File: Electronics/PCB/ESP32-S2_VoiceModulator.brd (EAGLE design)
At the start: 160 x 100 mm, 17 parts, among them IC1 ESP32-S2, IC2 AT25SF041-SSHD-B, J1 0532610671, Y1 FA-20H_40.0000MF15Z-AC3

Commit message: CHanged labelign for VCC/ power
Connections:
- new net VCC: C10.1, C11.1, C4.1, C5.1, C6.1, C7.1, C8.1, C9.1, IC1.1, IC1.3, IC1.4, IC1.45, IC1.51, IC1.54, IC2.8, R1.2, R2.2
- net +3V3: no longer C10.1, C11.1, C4.1, C5.1, C6.1, C7.1, C8.1, C9.1, IC1.1, IC1.3, IC1.4, IC1.45, IC1.51, IC1.54, IC2.8, R1.2, R2.2
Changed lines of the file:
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@@
 </signal>
 <signal name="+3V3">
-<contactref element="IC2" pad="8"/>
-<contactref element="C10" pad="1"/>
-<contactref element="R2" pad="2"/>
-<contactref element="C4" pad="1"/>
-<contactref element="C5" pad="1"/>
-<contactref element="C7" pad="1"/>
-<contactref element="C8" pad="1"/>
-<contactref element="C9" pad="1"/>
-<contactref element="C11" pad="1"/>
-<contactref element="C6" pad="1"/>
-<contactref element="IC1" pad="54"/>
-<contactref element="IC1" pad="51"/>
-<contactref element="IC1" pad="45"/>
 <contactref element="IC1" pad="20"/>
 <contactref element="IC1" pad="27"/>
 <contactref element="IC1" pad="30"/>
-<contactref element="IC1" pad="4"/>
-<contactref element="IC1" pad="3"/>
-<contactref element="IC1" pad="1"/>
-<contactref element="R1" pad="2"/>
-<wire x1="1.35" y1="-28" x2="1.35" y2="-33" width="0" layer="19" extent="1-1"/>
-<wire x1="1.35" y1="-23" x2="1.35" y2="-28" width="0" layer="19" extent="1-1"/>
-<wire x1="1.15" y1="-18" x2="1.35" y2="-23" width="0" layer="19" extent="1-1"/>
-<wire x1="4.4" y1="-8.45" x2="1.15" y2="-18" width="0" layer="19" extent="1-1"/>
 <wire x1="7.2" y1="-8.45" x2="4.4" y2="-8.45" width="0" layer="19" extent="1-1"/>
 <wire x1="8.45" y1="-7.2" x2="7.2" y2="-8.45" width="0" layer="19" extent="1-1"/>
-<wire x1="1.55" y1="-3.6" x2="4.4" y2="-8.45" width="0" layer="19" extent="1-1"/>
-<wire x1="1.55" y1="-3.2" x2="1.55" y2="-3.6" width="0" layer="19" extent="1-1"/>
-<wire x1="1.55" y1="-2.4" x2="1.55" y2="-3.2" width="0" layer="19" extent="1-1"/>
-<wire x1="3.2" y1="-1.55" x2="1.55" y2="-2.4" width="0" layer="19" extent="1-1"/>
-<wire x1="4.4" y1="-1.55" x2="3.2" y2="-1.55" width="0" layer="19" extent="1-1"/>
-<wire x1="6.8" y1="-1.55" x2="4.4" y2="-1.55" width="0" layer="19" extent="1-1"/>
-<wire x1="16.15" y1="-18" x2="7.2" y2="-8.45" width="0" layer="19" extent="1-1"/>
-<wire x1="16.35" y1="-23" x2="16.15" y2="-18" width="0" layer="19" extent="1-1"/>
-<wire x1="16.35" y1="-28" x2="16.35" y2="-23" width="0" layer="19" extent="1-1"/>
-<wire x1="16.35" y1="-33" x2="16.35" y2="-28" width="0" layer="19" extent="1-1"/>
-<wire x1="16.85" y1="-43" x2="16.35" y2="-33" width="0" layer="19" extent="1-1"/>
-<wire x1="24.85" y1="-43" x2="16.85" y2="-43" width="0" layer="19" extent="1-1"/>
-<wire x1="22.712" y1="-1.095" x2="8.45" y2="-7.2" width="0" layer="19" extent="1-1"/>
 </signal>
 <signal name="SPID">
@@
 <wire x1="1.55" y1="-4" x2="8.875" y2="-46.996" width="0" layer="19" extent="1-1"/>
 </signal>
+<signal name="VCC">
+<contactref element="IC1" pad="4"/>
+<contactref element="IC1" pad="3"/>
+<contactref element="IC1" pad="1"/>
+<contactref element="R1" pad="2"/>
+<contactref element="IC1" pad="54"/>
+<contactref element="IC1" pad="51"/>
+<contactref element="IC1" pad="45"/>
+<contactref element="R2" pad="2"/>
+<contactref element="IC2" pad="8"/>
+<contactref element="C10" pad="1"/>
+<contactref element="C4" pad="1"/>
+<contactref element="C5" pad="1"/>
+<contactref element="C7" pad="1"/>
+<contactref element="C8" pad="1"/>
+<contactref element="C9" pad="1"/>
+<contactref element="C11" pad="1"/>
+<contactref element="C6" pad="1"/>
+<wire x1="1.35" y1="-28" x2="1.35" y2="-33" width="0" layer="19" extent="1-1"/>
+<wire x1="1.35" y1="-23" x2="1.35" y2="-28" width="0" layer="19" extent="1-1"/>
+<wire x1="1.15" y1="-18" x2="1.35" y2="-23" width="0" layer="19" extent="1-1"/>
+<wire x1="1.55" y1="-3.6" x2="1.15" y2="-18" width="0" layer="19" extent="1-1"/>
+<wire x1="1.55" y1="-3.2" x2="1.55" y2="-3.6" width="0" layer="19" extent="1-1"/>
+<wire x1="1.55" y1="-2.4" x2="1.55" y2="-3.2" width="0" layer="19" extent="1-1"/>
+<wire x1="3.2" y1="-1.55" x2="1.55" y2="-2.4" width="0" layer="19" extent="1-1"/>
+<wire x1="4.4" y1="-1.55" x2="3.2" y2="-1.55" width="0" layer="19" extent="1-1"/>
+<wire x1="6.8" y1="-1.55" x2="4.4" y2="-1.55" width="0" layer="19" extent="1-1"/>
+<wire x1="16.35" y1="-33" x2="1.35" y2="-33" width="0" layer="19" extent="1-1"/>
+<wire x1="16.35" y1="-28" x2="16.35" y2="-33" width="0" layer="19" extent="1-1"/>
+<wire x1="16.35" y1="-23" x2="16.35" y2="-28" width="0" layer="19" extent="1-1"/>
+<wire x1="16.15" y1="-18" x2="16.35" y2="-23" width="0" layer="19" extent="1-1"/>
+<wire x1="16.85" y1="-43" x2="16.35" y2="-33" width="0" layer="19" extent="1-1"/>
+<wire x1="24.85" y1="-43" x2="16.85" y2="-43" width="0" layer="19" extent="1-1"/>
+<wire x1="22.712" y1="-1.095" x2="6.8" y2="-1.55" width="0" layer="19" extent="1-1"/>
+</signal>
 <signal name="+5V">

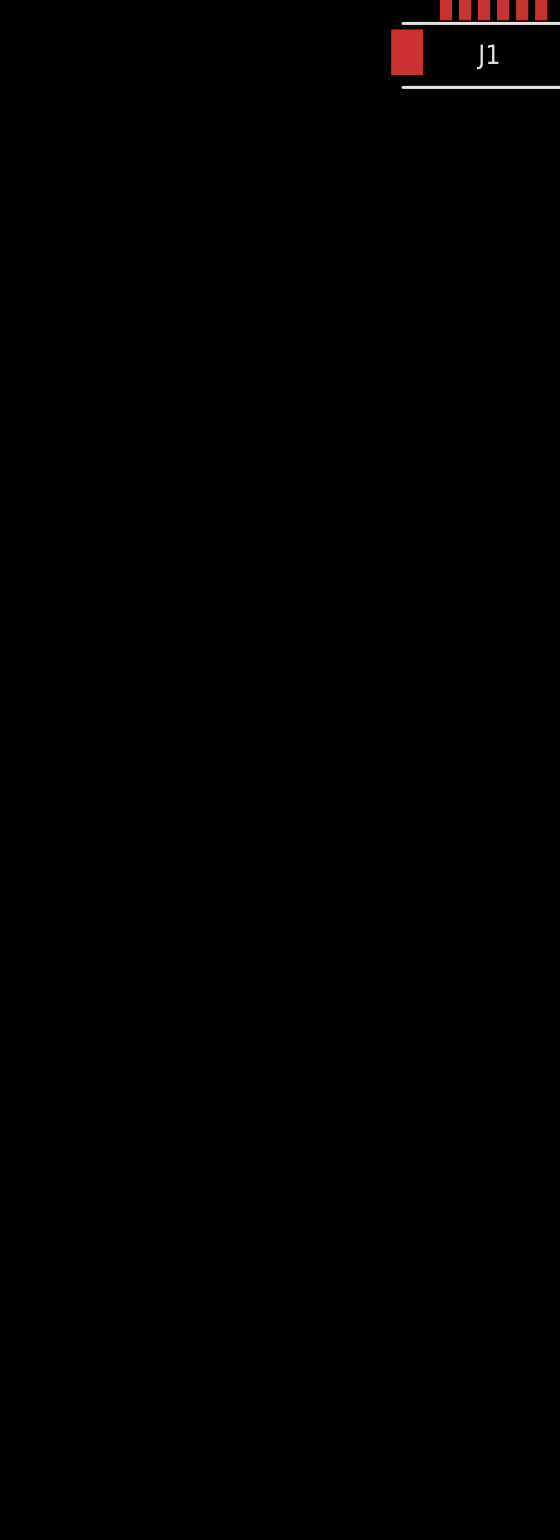
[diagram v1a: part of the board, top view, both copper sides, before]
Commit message: Added schematic drawing for the microphone emulation and PCB microphone adjustment.
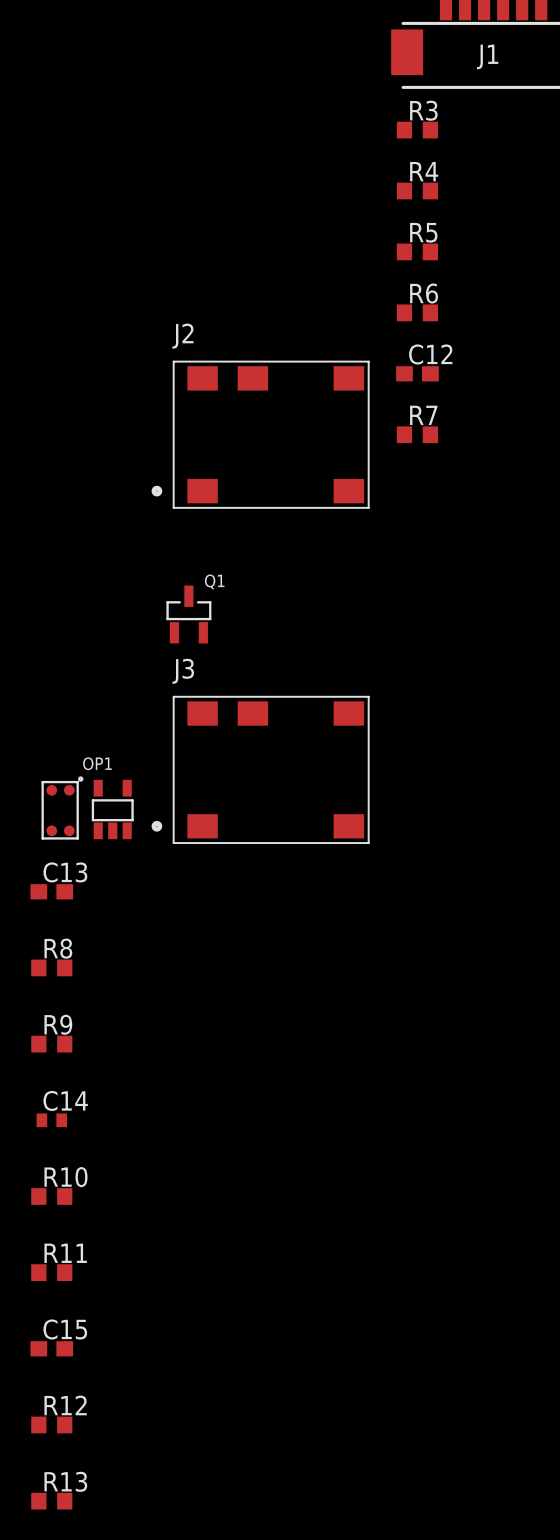
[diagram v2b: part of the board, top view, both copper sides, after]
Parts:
- added C12, C13, C15: 1uF/6.3V, resistor:C0603
- added C14: 0.1µF/16V, rcl:C0402
- added J2, J3: (no value), VoiceModulator:SJ2-35364B-SMT-TR
- added MK1: WMM7022AT0, VoiceModulator:WMM7022AT0
- added OP1: MCP6001T-I/OT, VoiceModulator:SOT-23-5
- added Q1: CPH3910, VoiceModulator:SOT-23-3
- added R10, R9: 1K, resistor:R0603
- added R11: 70k, resistor:R0603
- added R12, R13, R8: 100K, resistor:R0603
- added R3, R5, R6, R7: 10K, resistor:R0603
- added R4: 100R, resistor:R0603
- C1, C10, C11, C6, C7, C8, C9: value 0.1µF/16V/X7R -> 0.1µF/16V
- C2, C3: value 9pF/6.3V/X7R -> 9pF/6.3V
- C4, C5: value 10µF/6.3V/X7R -> 10µF/6.3V
- R1, R2: value 10K/5% -> 10K
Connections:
- new net AGND: J2.4, J3.4, Q1.P$1, R5.2
- new net AUDIO_LEFT: J2.2, J3.2
- new net AUDIO_RIGHT: J2.3, J3.3
- new net DAC_OUTPUT: R3.2
- new net HEADPHONE_SWITCH: J2.10
- new net MICROPHONE_HEADSET: J2.1
- new net MICROPHONE_OUT: J3.1, R6.1, R7.2
- new net N$1: C12.2, Q1.P$3, R5.1
- new net N$2: C12.1, R3.1, R4.2
- new net N$3: C13.2, OP1.P$3, R8.1, R9.2
- new net N$4: C13.1, MK1.4
- new net N$5: Q1.P$2, R6.2, R7.1
- new net N$6: OP1.P$4, R10.2, R11.2
- new net N$7: C15.1, OP1.P$1, R11.1
- new net PCB-MICROPHONE_OUTPUT: C15.2, R12.2, R13.1
- new net PHONE_SWITCH: J3.10
- net +5V: now also OP1.P$5
- net GND: now also C14.2, MK1.2, MK1.3, OP1.P$2, R10.1, R12.1, R4.1, R9.1
- net VCC: now also C14.1, MK1.1, R13.2, R8.2

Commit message: Added DC/DC
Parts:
- added C16, C17: 1uF/6.3V, resistor:C0603
- added IC3: MIC5504-3.3YM5-TR, VoiceModulator:SOT-23-5
- J2, J3: value (none) -> SJ2-35364B-SMT-TR
- moved OP1 57.9 mm to (-36.0, -156.0)
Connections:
- net +5V: now also C16.1, IC3.P$1, IC3.P$3
- net GND: now also C16.2, C17.2, IC3.P$2
- net VCC: now also C17.1, IC3.P$5
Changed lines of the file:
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@@
 <attribute name="VALUE" x="1.365" y="-76.905" size="1.27" layer="27"/>
 </element>
-<element name="J2" library="VoiceModulator" package="SJ2-35364B-SMT-TR" value="" x="-14" y="-75" smashed="yes">
+<element name="J2" library="VoiceModulator" package="SJ2-35364B-SMT-TR" value="SJ2-35364B-SMT-TR" x="-14" y="-75" smashed="yes">
 <attribute name="NAME" x="-14" y="-68.9989" size="1.27023125" layer="25"/>
 <attribute name="VALUE" x="-14" y="-81.002440625" size="1.27051875" layer="27" align="top-left"/>
@@
 <attribute name="NAME" x="-12" y="-85" size="0.8128" layer="25"/>
 </element>
-<element name="J3" library="VoiceModulator" package="SJ2-35364B-SMT-TR" value="" x="-14" y="-97" smashed="yes">
+<element name="J3" library="VoiceModulator" package="SJ2-35364B-SMT-TR" value="SJ2-35364B-SMT-TR" x="-14" y="-97" smashed="yes">
 <attribute name="NAME" x="-14" y="-90.9989" size="1.27023125" layer="25"/>
 <attribute name="VALUE" x="-14" y="-103.002440625" size="1.27051875" layer="27" align="top-left"/>
-</element>
-<element name="OP1" library="VoiceModulator" package="SOT-23-5" value="MCP6001T-I/OT" x="-18" y="-101" smashed="yes">
-<attribute name="NAME" x="-20" y="-97" size="0.8128" layer="25"/>
 </element>
 <element name="MK1" library="VoiceModulator" package="WMM7022AT0" value="WMM7022AT0" x="-22" y="-101" smashed="yes"/>
@@
 <attribute name="NAME" x="-22.635" y="-144.365" size="1.27" layer="25"/>
 <attribute name="VALUE" x="-22.635" y="-146.905" size="1.27" layer="27"/>
+</element>
+<element name="C16" library="resistor" library_urn="urn:adsk.eagle:library:348" package="C0603" package3d_urn="urn:adsk.eagle:package:23616/2" value="1uF/6.3V" x="-27" y="-150" smashed="yes">
+<attribute name="NAME" x="-27.635" y="-149.365" size="1.27" layer="25"/>
+<attribute name="VALUE" x="-27.635" y="-151.905" size="1.27" layer="27"/>
+</element>
+<element name="C17" library="resistor" library_urn="urn:adsk.eagle:library:348" package="C0603" package3d_urn="urn:adsk.eagle:package:23616/2" value="1uF/6.3V" x="-27" y="-155" smashed="yes">
+<attribute name="NAME" x="-27.635" y="-154.365" size="1.27" layer="25"/>
+<attribute name="VALUE" x="-27.635" y="-156.905" size="1.27" layer="27"/>
+</element>
+<element name="IC3" library="VoiceModulator" package="SOT-23-5" value="MIC5504-3.3YM5-TR" x="-31" y="-156" smashed="yes">
+<attribute name="NAME" x="-33" y="-152" size="0.8128" layer="25"/>
+</element>
+<element name="OP1" library="VoiceModulator" package="SOT-23-5" value="MCP6001T-I/OT" x="-36" y="-156" smashed="yes">
+<attribute name="NAME" x="-38" y="-152" size="0.8128" layer="25"/>
 </element>
 </elements>
@@
 <contactref element="C14" pad="2"/>
 <contactref element="R10" pad="1"/>
+<contactref element="R12" pad="1"/>
+<contactref element="C16" pad="2"/>
+<contactref element="C17" pad="2"/>
+<contactref element="IC3" pad="P$2"/>
 <contactref element="OP1" pad="P$2"/>
-<contactref element="R12" pad="1"/>
+<wire x1="-31" y1="-156" x2="-36" y2="-156" width="0" layer="19" extent="1-1"/>
+<wire x1="-26.15" y1="-155" x2="-31" y2="-156" width="0" layer="19" extent="1-1"/>
+<wire x1="-26.15" y1="-150" x2="-26.15" y2="-155" width="0" layer="19" extent="1-1"/>
+<wire x1="-22.85" y1="-140" x2="-26.15" y2="-150" width="0" layer="19" extent="1-1"/>
 <wire x1="-22.85" y1="-125" x2="-22.85" y2="-140" width="0" layer="19" extent="1-1"/>
 <wire x1="-21.35" y1="-120" x2="-22.85" y2="-125" width="0" layer="19" extent="1-1"/>
@@
 <wire x1="-22" y1="-101" x2="-22.85" y2="-115" width="0" layer="19" extent="1-1"/>
 <wire x1="-20.85" y1="-101" x2="-22" y2="-101" width="0" layer="19" extent="1-1"/>
-<wire x1="-18" y1="-101" x2="-20.85" y2="-101" width="0" layer="19" extent="1-1"/>
-<wire x1="1.15" y1="-59" x2="-18" y2="-101" width="0" layer="19" extent="1-1"/>
+<wire x1="1.15" y1="-59" x2="-20.85" y2="-101" width="0" layer="19" extent="1-1"/>
 <wire x1="10.125" y1="-46.996" x2="1.15" y2="-59" width="0" layer="19" extent="1-1"/>
 <wire x1="2.85" y1="-43" x2="10.125" y2="-46.996" width="0" layer="19" extent="1-1"/>
@@
 <contactref element="IC1" pad="51"/>
 <contactref element="IC1" pad="45"/>
-<contactref element="R2" pad="2"/>
 <contactref element="IC2" pad="8"/>
 <contactref element="C10" pad="1"/>
@@
 <contactref element="C14" pad="1"/>
 <contactref element="R13" pad="2"/>
+<contactref element="C17" pad="1"/>
+<contactref element="IC3" pad="P$5"/>
+<contactref element="R2" pad="2"/>
+<wire x1="-27.85" y1="-155" x2="-31.95" y2="-153.2" width="0" layer="19" extent="1-1"/>
+<wire x1="-21.15" y1="-145" x2="-27.85" y2="-155" width="0" layer="19" extent="1-1"/>
 <wire x1="-22.65" y1="-120" x2="-21.15" y2="-145" width="0" layer="19" extent="1-1"/>
 <wire x1="-21.15" y1="-110" x2="-22.65" y2="-120" width="0" layer="19" extent="1-1"/>
@@
 <signal name="+5V">
 <contactref element="J1" pad="1"/>
+<contactref element="C16" pad="1"/>
+<contactref element="IC3" pad="P$1"/>
+<contactref element="IC3" pad="P$3"/>
 <contactref element="OP1" pad="P$5"/>
-<wire x1="3.875" y1="-46.996" x2="-18.95" y2="-98.2" width="0" layer="19" extent="1-1"/>
+<wire x1="-31.95" y1="-156" x2="-36.95" y2="-153.2" width="0" layer="19" extent="1-1"/>
+<wire x1="-30.05" y1="-156" x2="-31.95" y2="-156" width="0" layer="19" extent="1-1"/>
+<wire x1="-27.85" y1="-150" x2="-30.05" y2="-156" width="0" layer="19" extent="1-1"/>
+<wire x1="3.875" y1="-46.996" x2="-27.85" y2="-150" width="0" layer="19" extent="1-1"/>
 </signal>
 <signal name="N$1">
@@
 <contactref element="R9" pad="2"/>
 <contactref element="OP1" pad="P$3"/>
+<wire x1="-21.15" y1="-115" x2="-35.05" y2="-156" width="0" layer="19" extent="1-1"/>
 <wire x1="-22.85" y1="-110" x2="-21.15" y2="-115" width="0" layer="19" extent="1-1"/>
 <wire x1="-21.15" y1="-105" x2="-22.85" y2="-110" width="0" layer="19" extent="1-1"/>
-<wire x1="-17.05" y1="-101" x2="-21.15" y2="-105" width="0" layer="19" extent="1-1"/>
 </signal>
 <signal name="N$6">
 <contactref element="R10" pad="2"/>
+<contactref element="R11" pad="2"/>
 <contactref element="OP1" pad="P$4"/>
-<contactref element="R11" pad="2"/>
+<wire x1="-21.15" y1="-130" x2="-35.05" y2="-153.2" width="0" layer="19" extent="1-1"/>
 <wire x1="-21.15" y1="-125" x2="-21.15" y2="-130" width="0" layer="19" extent="1-1"/>
-<wire x1="-17.05" y1="-98.2" x2="-21.15" y2="-125" width="0" layer="19" extent="1-1"/>
 </signal>
 <signal name="N$7">
 <contactref element="R11" pad="1"/>
+<contactref element="C15" pad="1"/>
 <contactref element="OP1" pad="P$1"/>
-<contactref element="C15" pad="1"/>
+<wire x1="-22.85" y1="-135" x2="-36.95" y2="-156" width="0" layer="19" extent="1-1"/>
 <wire x1="-22.85" y1="-130" x2="-22.85" y2="-135" width="0" layer="19" extent="1-1"/>
-<wire x1="-18.95" y1="-101" x2="-22.85" y2="-130" width="0" layer="19" extent="1-1"/>
 </signal>
 <signal name="PCB-MICROPHONE_OUTPUT">

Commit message: Minor changes to schematic
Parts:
- removed J1: 0532610671, SamacSys_Parts:0532610671
- added C18: 0.1µF/16V, resistor:C0603
- added C19: 0.1µF/16V, rcl:C0402
- added C20: 1uF/6.3V, resistor:C0603
- added C21: 10µF/6.3V, rcl:C0603
- added J4: 10118192-0002LF, VoiceModulator:CONN_10118192-0002LF_AMP
- added OP2: MCP6001T-I/OT, VoiceModulator:SOT-23-5
- added R14, R18, R19, R20: 100K, resistor:R0603
- added R15, R16: 1K, resistor:R0603
- added R17: 70k, resistor:R0603
- added TAG_CONNECT_ICSP_HEADER: TAG-CONNECT_PADS, TAG-CONNECT_PADS-lbr:TAG-CONNECT_PADS
- R3: value 10K -> 100K
- R4: value 100R -> 1k
- moved C16 204.2 mm to (-19.0, 54.0)
- moved C17 204.2 mm to (-19.0, 49.0)
- moved OP1 184.6 mm to (13.0, 22.0)
- moved R13 177.3 mm to (-12.0, 32.0)
- moved C15 172.1 mm to (-15.0, 37.0)
- moved R12 172.0 mm to (-18.0, 32.0)
- moved IC3 171.9 mm to (19.7, 8.30), turned to 90 degrees
- moved C14 164.0 mm to (-20.0, 44.0)
- moved R11 157.0 mm to (-19.0, 27.0)
- moved R10 152.0 mm to (-24.0, 27.0)
- moved J3 144.5 mm to (7.00, 46.0), turned to 270 degrees
- moved R9 142.2 mm to (-14.0, 27.0)
- moved R8 142.0 mm to (-24.0, 32.0)
- moved C13 130.4 mm to (15.0, 20.0), turned to 90 degrees
- moved MK1 126.4 mm to (11.0, 21.0), turned to 270 degrees
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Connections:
- removed net AGND: J2.4, J3.4, Q1.P$1, R5.2
- new net D+: IC1.25, J4.3
- new net D-: IC1.26, J4.2
- new net EXTERNAL-MICROPHONE_OUTPUT: C20.2, R18.2, R19.1
- new net ID: J4.4
- new net N$10: OP2.P$4, R16.2, R17.2
- new net N$11: C20.1, OP2.P$1, R17.1
- new net N$9: C18.2, OP2.P$3, R14.1, R15.2
- net +5V: now also C21.1, J4.1, OP2.P$5, TAG_CONNECT_ICSP_HEADER.MISO; no longer J1.1
- net EN: now also TAG_CONNECT_ICSP_HEADER.VCC; no longer J1.4
- net GND: now also C19.2, C21.2, J2.4, J3.4, J4.5, OP2.P$2, Q1.P$1, R15.1, R16.1, R18.1, R5.2, TAG_CONNECT_ICSP_HEADER.GND; no longer J1.6
- net I/O0: now also TAG_CONNECT_ICSP_HEADER.MOSI; no longer J1.5
- net MICROPHONE_HEADSET: now also C18.1, C19.1, R20.1
- net RXD0: now also TAG_CONNECT_ICSP_HEADER.RST; no longer J1.3
- net TXD0: now also TAG_CONNECT_ICSP_HEADER.SCK; no longer J1.2
- net VCC: now also R14.2, R19.2, R20.2
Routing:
- net GND: track 0.00 -> 6.69 mm
- net N$5: track 0.00 -> 4.74 mm
- net N$1: track 0.00 -> 4.62 mm
- net N$2: track 0.00 -> 3.50 mm
- net +5V: track 0.00 -> 2.15 mm
- net AUDIO_RIGHT: track 0.00 -> 2.01 mm
- added copper zone on layer 1, net GND
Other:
- board size 160 x 100 mm -> 27 x 46 mm

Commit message: Minor changes
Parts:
- added R21, R22, R23, R24: 10K, resistor:R0603
- added S1, S2, S3, S4: PTS647SK70SMTR2LFS, VoiceModulator:PTS647SKXXSMTR2LFS
- moved MK1 12.2 mm to (4.00, 31.0)
- moved C13 10.4 mm to (5.00, 23.0)
- moved C12 9.49 mm to (9.60, 38.2)
- moved Q1 9.49 mm to (4.80, 35.7)
- moved R5 9.49 mm to (6.00, 38.2)
- moved R3 9.49 mm to (9.60, 36.1)
- moved R4 9.49 mm to (12.7, 36.1)
- moved OP1 8.06 mm to (9.00, 29.0)
- moved IC1 8.00 mm to (21.0, 45.0)
- moved IC2 8.00 mm to (22.0, 37.0)
- moved J3 8.00 mm to (7.00, 54.0)
- moved TAG_CONNECT_ICSP_HEADER 8.00 mm to (14.0, 50.0)
- moved Y1 8.00 mm to (19.0, 51.0)
- moved R6 5.39 mm to (4.00, 32.7)
- moved R7 5.39 mm to (1.90, 32.7)
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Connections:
- new net SW_1: R21.2, S1.3, S1.4
- new net SW_2: R22.2, S2.3, S2.4
- new net SW_3: R23.2, S3.3, S3.4
- new net SW_4: R24.2, S4.3, S4.4
- net GND: now also S1.1, S1.2, S2.1, S2.2, S3.1, S3.2, S4.1, S4.2
- net VCC: now also R21.1, R22.1, R23.1, R24.1
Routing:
- net GND: track 6.69 -> 1.55 mm
- net N$5: track 4.74 -> 2.10 mm
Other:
- board size 27 x 46 mm -> 27 x 54 mm
